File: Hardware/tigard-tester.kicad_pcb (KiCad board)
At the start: 2 copper layers, 50 x 100 mm, 119 parts, among them J1 UART, J2 JTAG, J3 SPI, J4 LA, J5 I2C

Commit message: hardware finished
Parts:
- added H1: MountingHole, MountingHole:MountingHole_3.2mm_M3, F.Cu at (101.0, 43.0)
- added H2: MountingHole, MountingHole:MountingHole_3.2mm_M3, F.Cu at (145.0, 43.0)
- added H3: MountingHole, MountingHole:MountingHole_3.2mm_M3, F.Cu at (101.0, 137.2)
- added H4: MountingHole, MountingHole:MountingHole_3.2mm_M3, F.Cu at (145.0, 137.0)
- moved D37 1.27 mm to (116.8, 130.8)
- moved D38 1.27 mm to (116.8, 133.3)
- moved R37 1.27 mm to (111.8, 130.8)
- moved R38 1.27 mm to (111.8, 133.3)
- moved kibuzzard-6782A18A 1.27 mm to (114.3, 135.9)
- moved kibuzzard-6782A634 1.27 mm to (127.0, 130.8)
- moved kibuzzard-6782A63C 1.27 mm to (127.0, 133.3)
- moved kibuzzard-6782A58D 1.27 mm to (123.2, 106.7)
- moved kibuzzard-6782A593 1.27 mm to (123.2, 109.2)
- moved kibuzzard-6782A59C 1.27 mm to (123.2, 111.8)
- moved kibuzzard-6782A5EC 1.27 mm to (123.2, 114.3)
- moved D36 1.27 mm to (116.8, 128.3)
- moved J5 1.27 mm to (106.7, 128.3)
- moved R36 1.27 mm to (111.8, 128.3)
- moved kibuzzard-6782A62E 1.27 mm to (127.0, 128.3)
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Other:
- outline, holes or cut-outs redrawn
- board text added: "I2C"
- board text added: "JTAG"
- board text added: "LA"
- board text added: "SPI"
- board text added: "Tigard Tester"
- board text added: "UART"
- board text added: "v1.0 @casartar 2025"

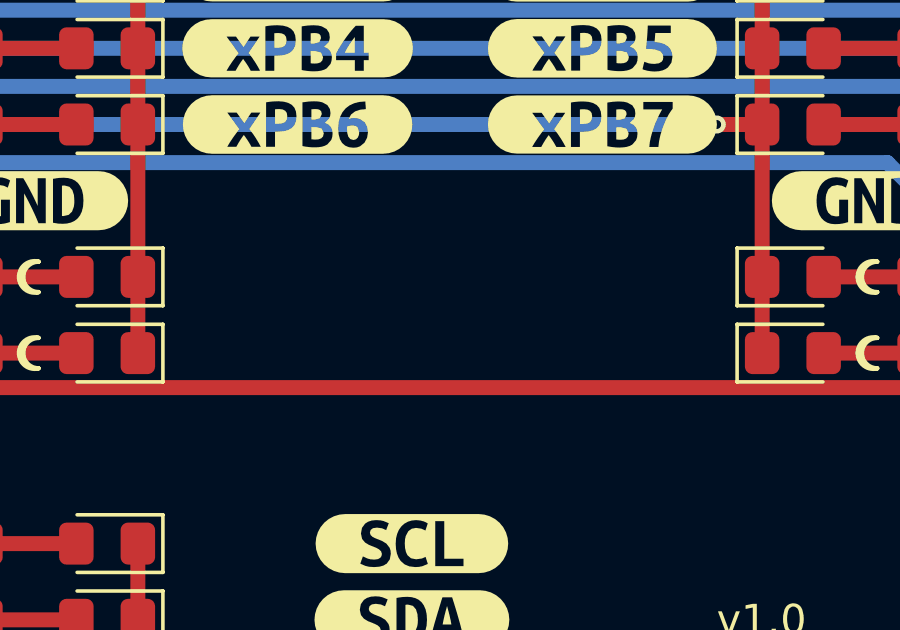
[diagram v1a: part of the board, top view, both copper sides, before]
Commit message: n.c. added
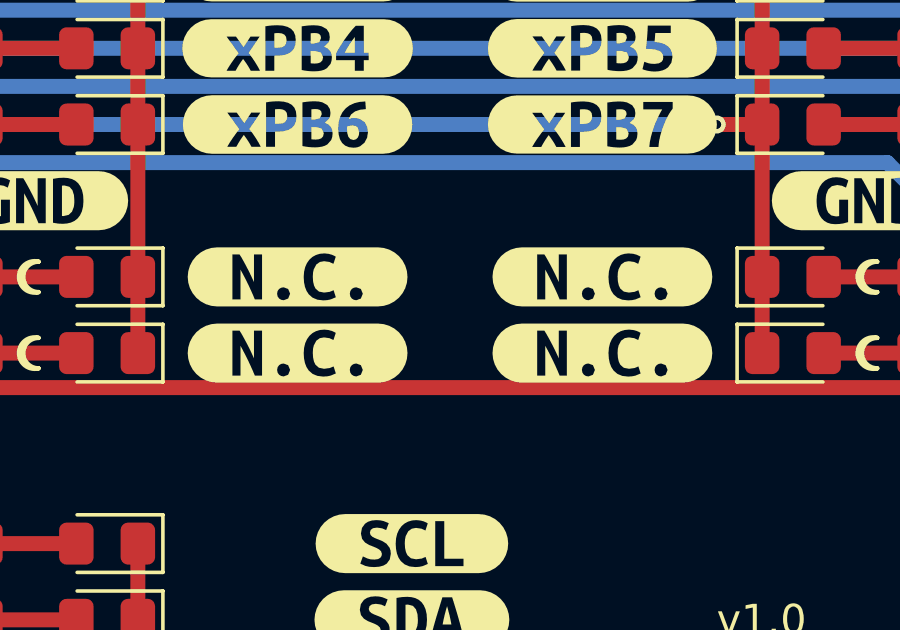
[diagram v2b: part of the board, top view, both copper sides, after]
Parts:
- added kibuzzard-6782BFBD: G***, kibuzzard-6782BFBD, F.Cu at (123.2, 119.4)
- added kibuzzard-6782BFBD: G***, kibuzzard-6782BFBD, F.Cu at (123.2, 121.9)
- added kibuzzard-6782BFBD: G***, kibuzzard-6782BFBD, F.Cu at (133.3, 121.9)
- added kibuzzard-6782BFBD: G***, kibuzzard-6782BFBD, F.Cu at (133.3, 119.4)
